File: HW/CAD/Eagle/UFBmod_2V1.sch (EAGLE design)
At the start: 200 parts, among them J1411 ABRACON_ARJE-0034, T0551 MMBT2222, U0501 MIDAS_MCCOG21605B6W-FPTLWI, U0601 MAX5217, U0701 AT86RF215-ZU, U0711 ASVTX-13-D-26.000MHZ-I05-T, U0811 PE4259, U0821 RFX1010, U0881 B39871B3440U410, U0911 FT232HL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

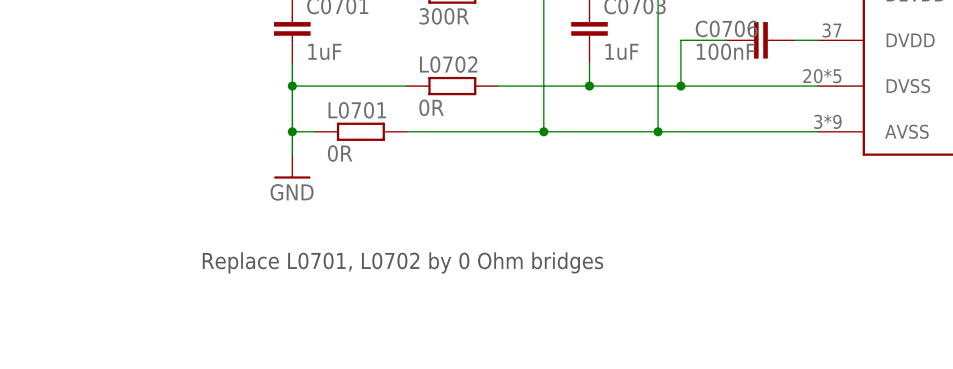
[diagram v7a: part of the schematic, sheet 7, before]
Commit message: HW - Eagle - V2.1 V2.2 - Remarks for RF09 BALUN replacement
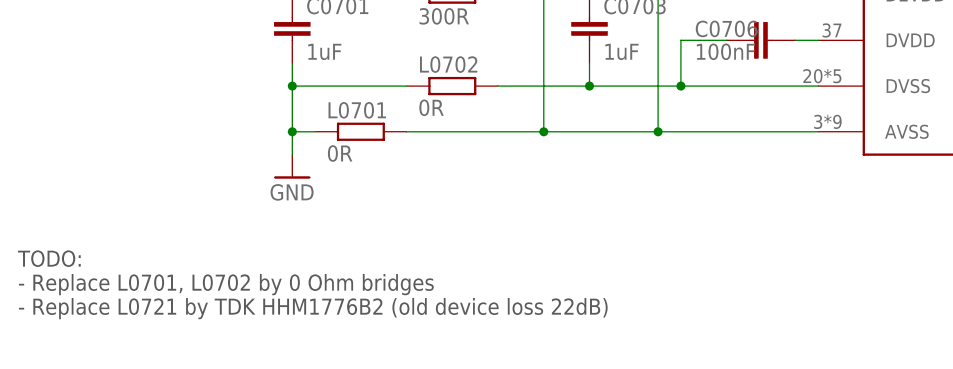
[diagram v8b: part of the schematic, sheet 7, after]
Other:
- note added: "TODO: - Replace L0701, L0702 by 0 Ohm bridges - Replace L0721 by TDK HHM1776B2 (old device loss 22dB)"
- note removed: "Replace L0701, L0702 by 0 Ohm bridges"
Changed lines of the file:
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@@
 <text x="22.86" y="162.56" size="2.54" layer="97" ratio="15">Microchip Technologies AT86RF215</text>
 <text x="93.98" y="83.82" size="1.778" layer="97">26MHz</text>
-<text x="35.56" y="22.86" size="1.778" layer="97">Replace L0701, L0702 by 0 Ohm bridges</text>
+<text x="15.24" y="17.78" size="1.778" layer="97">TODO:
+- Replace L0701, L0702 by 0 Ohm bridges
+- Replace L0721 by TDK HHM1776B2 (old device loss 22dB)</text>
 </plain>
 <instances>
